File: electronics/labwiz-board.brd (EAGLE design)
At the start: 98.8 x 51 mm, 92 parts, among them J1 SD_MICRO_SDIO_1BIT, J2 CORTEX_DEBUGSMD, J3 DNP, U1 STM32F10XRXT6, U2 MCP73831, U4 MIC5219-3.3V, X2 M12_BOTTOM_CONTACTS_FPC_1MM, Y3 32.768kHz

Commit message: Updated .gitignore. Comitting unknown schematic updates.
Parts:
- removed J4: (no value), SparkFun-Connectors:1X03
- added TP10, TP8, TP9: DNP, PaxInstruments-Connectors:PAD_1MM
- moved BAT1 84.3 mm to (89.5, 16.7), turned to 90 degrees
- moved R19 19.9 mm to (37.0, 3.81), turned to 180 degrees
- moved U$6 18.6 mm to (48.6, 20.4)
- moved C3 14.6 mm to (91.1, 35.2), turned to 270 degrees
- moved TP3 13.0 mm to (83.9, 9.98)
- moved C31 7.63 mm to (8.08, 33.1)
- moved R15 7.63 mm to (8.08, 31.9)
- moved C30 4.57 mm to (8.08, 30.6)
- moved R16 4.57 mm to (8.08, 29.4)
- moved C35 4.28 mm to (37.0, 14.2), turned to 180 degrees
- moved R20 2.93 mm to (87.5, 35.2), turned to 90 degrees
- moved C36 2.89 mm to (37.0, 13.0), turned to 0 degrees
- moved C28 2.66 mm to (90.4, 18.3)
- moved R24 2.51 mm to (90.4, 17.1)
- moved C10 2.46 mm to (37.0, 11.7), turned to 0 degrees
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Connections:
- net GND: now also TP10.P$1; no longer J4.3
- net USART1_RX: now also TP9.P$1; no longer J4.2
- net USART1_TX: now also TP8.P$1; no longer J4.1
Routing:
- net LCD_BL: track 41.9 -> 18.0 mm
- net RTC_BAT: track 51.8 -> 70.1 mm, vias 1 -> 3
- net N$4: track 11.8 -> 25.7 mm
- net SWDIO: track 104.9 -> 117.3 mm
- net SWCLK: track 103.5 -> 115.2 mm
- net USART1_RX: track 107.5 -> 116.3 mm
- net I2C1_SCL: track 101.5 -> 109.4 mm
- net I2C1_SDA: track 101.5 -> 109.3 mm
- net USART2_TX: track 63.7 -> 71.5 mm, vias 5 -> 3
- net USART2_RX: track 57.2 -> 63.8 mm, vias 2 -> 4
- net SW_E_BOOT0: track 56.6 -> 50.2 mm
- net SW_A: track 113.3 -> 119.6 mm, vias 3 -> 5
- net N$38: track 4.33 -> 10.5 mm
- net N$37: track 4.76 -> 9.06 mm
- net NRST: track 125.7 -> 129.7 mm, vias 6 -> 5
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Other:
- outline, holes or cut-outs redrawn

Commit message: Updated MCP73831/2 name.
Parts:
- U2: value MCP73831 -> MCP73831/2
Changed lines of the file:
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@@
 <layer number="106" name="bPlate" color="7" fill="1" visible="yes" active="yes"/>
 <layer number="107" name="Crop" color="7" fill="1" visible="yes" active="yes"/>
+<layer number="108" name="tplace-old" color="7" fill="1" visible="yes" active="yes"/>
+<layer number="109" name="ref-old" color="7" fill="1" visible="yes" active="yes"/>
+<layer number="110" name="fp0" color="7" fill="1" visible="yes" active="yes"/>
+<layer number="111" name="LPC17xx" color="7" fill="1" visible="yes" active="yes"/>
+<layer number="112" name="tSilk" color="7" fill="1" visible="yes" active="yes"/>
+<layer number="113" name="ReferenceLS" color="7" fill="1" visible="yes" active="yes"/>
+<layer number="114" name="FRNTMAAT1" color="7" fill="1" visible="no" active="no"/>
+<layer number="115" name="FRNTMAAT2" color="7" fill="1" visible="no" active="no"/>
+<layer number="116" name="Patch_BOT" color="7" fill="1" visible="yes" active="yes"/>
 <layer number="117" name="BACKMAAT1" color="7" fill="1" visible="no" active="no"/>
+<layer number="118" name="Rect_Pads" color="7" fill="1" visible="yes" active="yes"/>
 <layer number="119" name="KAP_TEKEN" color="7" fill="1" visible="no" active="no"/>
 <layer number="120" name="KAP_MAAT1" color="7" fill="1" visible="no" active="no"/>
+<layer number="121" name="_tsilk" color="7" fill="1" visible="yes" active="yes"/>
+<layer number="122" name="_bsilk" color="7" fill="1" visible="yes" active="yes"/>
+<layer number="123" name="tTestmark" color="7" fill="1" visible="yes" active="yes"/>
+<layer number="124" name="bTestmark" color="7" fill="1" visible="yes" active="yes"/>
+<layer number="125" name="_tNames" color="7" fill="1" visible="yes" active="yes"/>
+<layer number="126" name="_bNames" color="7" fill="1" visible="yes" active="yes"/>
+<layer number="127" name="_tValues" color="7" fill="1" visible="yes" active="yes"/>
+<layer number="128" name="_bValues" color="7" fill="1" visible="yes" active="yes"/>
+<layer number="129" name="Mask" color="7" fill="1" visible="yes" active="yes"/>
 <layer number="130" name="SMDSTROOK" color="7" fill="1" visible="no" active="no"/>
+<layer number="131" name="tAdjust" color="7" fill="1" visible="yes" active="yes"/>
+<layer number="132" name="bAdjust" color="7" fill="1" visible="yes" active="yes"/>
 <layer number="133" name="bottom_silk" color="7" fill="1" visible="no" active="no"/>
+<layer number="144" name="Drill_legend" color="7" fill="1" visible="yes" active="yes"/>
+<layer number="150" name="Notes" color="7" fill="1" visible="yes" active="yes"/>
+<layer number="151" name="HeatSink" color="7" fill="1" visible="yes" active="yes"/>
+<layer number="152" name="_bDocu" color="7" fill="1" visible="yes" active="yes"/>
+<layer number="153" name="FabDoc1" color="7" fill="1" visible="yes" active="yes"/>
+<layer number="154" name="FabDoc2" color="7" fill="1" visible="yes" active="yes"/>
+<layer number="155" name="FabDoc3" color="7" fill="1" visible="yes" active="yes"/>
+<layer number="199" name="Contour" color="7" fill="1" visible="yes" active="yes"/>
+<layer number="200" name="200bmp" color="7" fill="1" visible="yes" active="yes"/>
+<layer number="201" name="201bmp" color="7" fill="1" visible="yes" active="yes"/>
+<layer number="202" name="202bmp" color="7" fill="1" visible="yes" active="yes"/>
+<layer number="203" name="203bmp" color="7" fill="1" visible="yes" active="yes"/>
+<layer number="204" name="204bmp" color="7" fill="1" visible="yes" active="yes"/>
+<layer number="205" name="205bmp" color="7" fill="1" visible="yes" active="yes"/>
+<layer number="206" name="206bmp" color="7" fill="1" visible="yes" active="yes"/>
+<layer number="207" name="207bmp" color="7" fill="1" visible="yes" active="yes"/>
+<layer number="208" name="208bmp" color="7" fill="1" visible="yes" active="yes"/>
+<layer number="209" name="209bmp" color="7" fill="1" visible="yes" active="yes"/>
+<layer number="210" name="210bmp" color="7" fill="1" visible="yes" active="yes"/>
+<layer number="211" name="211bmp" color="7" fill="1" visible="yes" active="yes"/>
+<layer number="212" name="212bmp" color="7" fill="1" visible="yes" active="yes"/>
+<layer number="213" name="213bmp" color="7" fill="1" visible="yes" active="yes"/>
+<layer number="214" name="214bmp" color="7" fill="1" visible="yes" active="yes"/>
+<layer number="215" name="215bmp" color="7" fill="1" visible="yes" active="yes"/>
+<layer number="216" name="216bmp" color="7" fill="1" visible="yes" active="yes"/>
 <layer number="217" name="217bmp" color="18" fill="1" visible="no" active="no"/>
 <layer number="218" name="218bmp" color="19" fill="1" visible="no" active="no"/>
@@
 <layer number="223" name="223bmp" color="24" fill="1" visible="no" active="no"/>
 <layer number="224" name="224bmp" color="25" fill="1" visible="no" active="no"/>
+<layer number="225" name="225bmp" color="7" fill="1" visible="yes" active="yes"/>
+<layer number="226" name="226bmp" color="7" fill="1" visible="yes" active="yes"/>
+<layer number="227" name="227bmp" color="7" fill="1" visible="yes" active="yes"/>
+<layer number="228" name="228bmp" color="7" fill="1" visible="yes" active="yes"/>
+<layer number="229" name="229bmp" color="7" fill="1" visible="yes" active="yes"/>
+<layer number="230" name="230bmp" color="7" fill="1" visible="yes" active="yes"/>
+<layer number="231" name="Eagle3D_PG1" color="7" fill="1" visible="yes" active="yes"/>
+<layer number="232" name="Eagle3D_PG2" color="7" fill="1" visible="yes" active="yes"/>
+<layer number="233" name="Eagle3D_PG3" color="7" fill="1" visible="yes" active="yes"/>
+<layer number="248" name="Housing" color="7" fill="1" visible="yes" active="yes"/>
+<layer number="249" name="Edge" color="7" fill="1" visible="yes" active="yes"/>
 <layer number="250" name="Descript" color="3" fill="1" visible="no" active="no"/>
 <layer number="251" name="SMDround" color="12" fill="11" visible="no" active="no"/>
+<layer number="254" name="cooling" color="7" fill="1" visible="yes" active="yes"/>
+<layer number="255" name="routoute" color="7" fill="1" visible="yes" active="yes"/>
 </layers>
 <board>
@@
 </element>
 <element name="U$9" library="PaxInstruments-FreqCtrl" package="NX3225GD" value="8MHz" x="33.8328" y="10.0584" smashed="yes" rot="R90"/>
-<element name="U2" library="PaxInstruments-PowerIC" package="SOT23-5" value="MCP73831" x="10.2108" y="2.286" smashed="yes" rot="R90">
+<element name="U2" library="PaxInstruments-PowerIC" package="SOT23-5" value="MCP73831/2" x="10.2108" y="2.286" smashed="yes" rot="R90">
 <attribute name="MPN" value="MCP73832T-2DCI/OT" x="10.2108" y="2.286" size="1.778" layer="27" rot="R90" display="off"/>
 <attribute name="MF" value="Microchip Technology" x="10.2108" y="2.286" size="1.778" layer="27" rot="R90" display="off"/>

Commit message: Swapped the net names for SW_D and SW_E. The physical locations were swapped on the v0.3 board.
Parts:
- R21: value 10K -> 2.32K (1%)
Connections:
- net SW_D_BOOT1 renamed SW_E_BOOT1
- net SW_E_BOOT0 renamed SW_D_BOOT0
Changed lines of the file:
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@@
 <attribute name="NAME" x="8.2296" y="2.286" size="0.5" layer="25" font="vector" align="center-left"/>
 </element>
-<element name="R21" library="PaxInstruments-RCL" package="0402" value="10K" x="14.3256" y="0.762" smashed="yes">
+<element name="R21" library="PaxInstruments-RCL" package="0402" value="2.32K (1%)" x="14.3256" y="0.762" smashed="yes">
 <attribute name="MPN" value="" x="14.3256" y="0.762" size="1.778" layer="27" display="off"/>
 <attribute name="POPULATE" value="" x="14.3256" y="0.762" size="1.778" layer="27" display="off"/>
@@
 <signal name="N$32">
 </signal>
-<signal name="SW_E_BOOT0">
+<signal name="SW_D_BOOT0">
 <contactref element="JP1" pad="1"/>
 <contactref element="U1" pad="29"/>
@@
 <wire x1="27.8892" y1="2.286" x2="51.5112" y2="2.286" width="0.1524" layer="16"/>
 </signal>
-<signal name="SW_D_BOOT1">
+<signal name="SW_E_BOOT1">
 <contactref element="U1" pad="28"/>
 <contactref element="R16" pad="2"/>

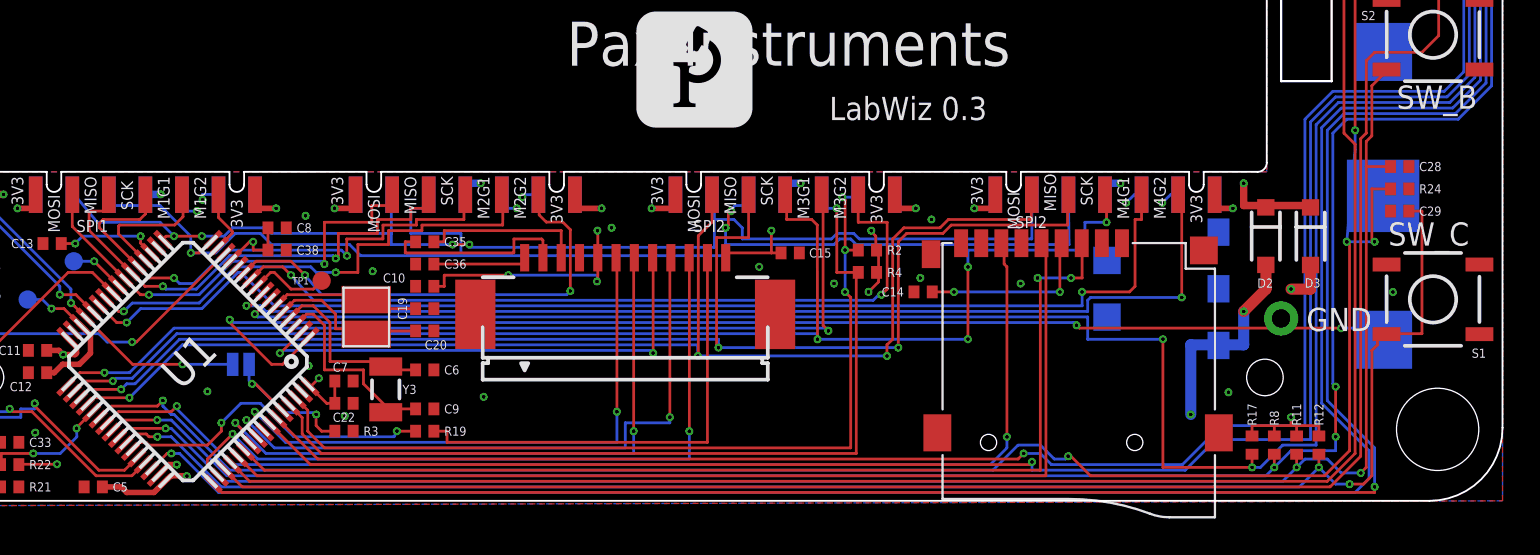
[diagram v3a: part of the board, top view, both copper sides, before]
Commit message: Swapped WIFI_EN with SW_A to avoid interrupt sharing.
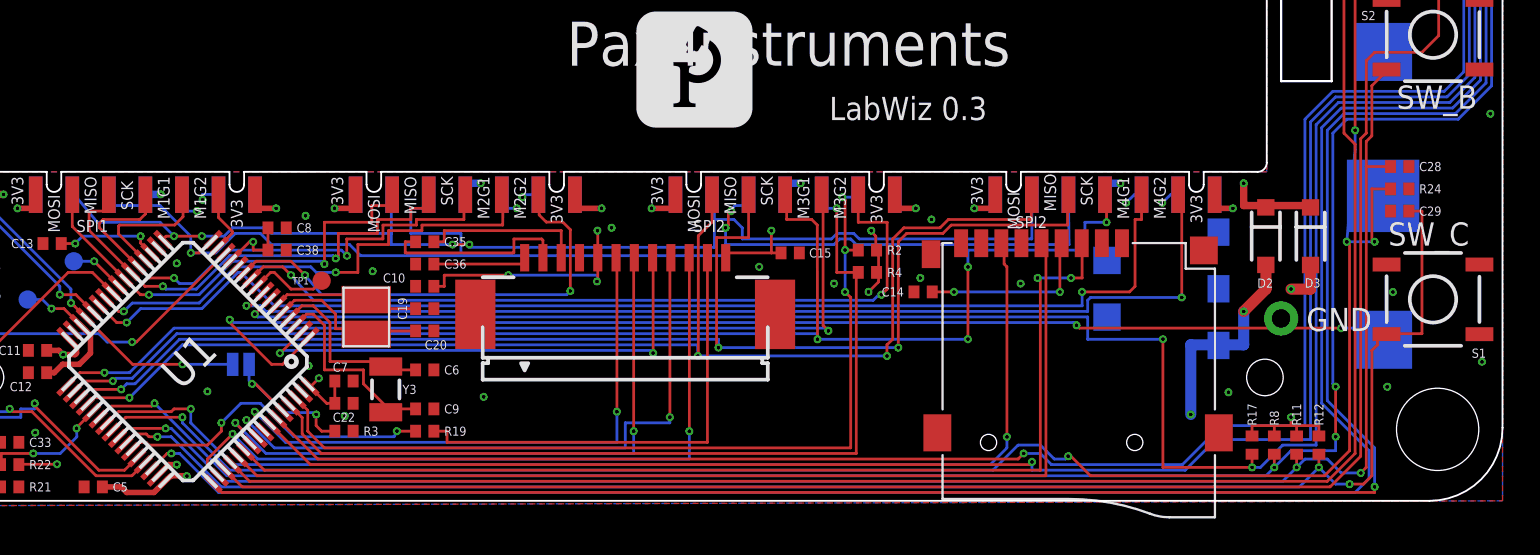
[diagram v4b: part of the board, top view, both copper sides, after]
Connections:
- net SW_A: now also U1.38; no longer U1.40
- net WIFI_EN: now also U1.40; no longer U1.38
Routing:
- net SW_A: track 119.6 -> 120.8 mm
- net WIFI_EN: track 108.7 -> 107.5 mm
- net GND: vias 23 -> 27

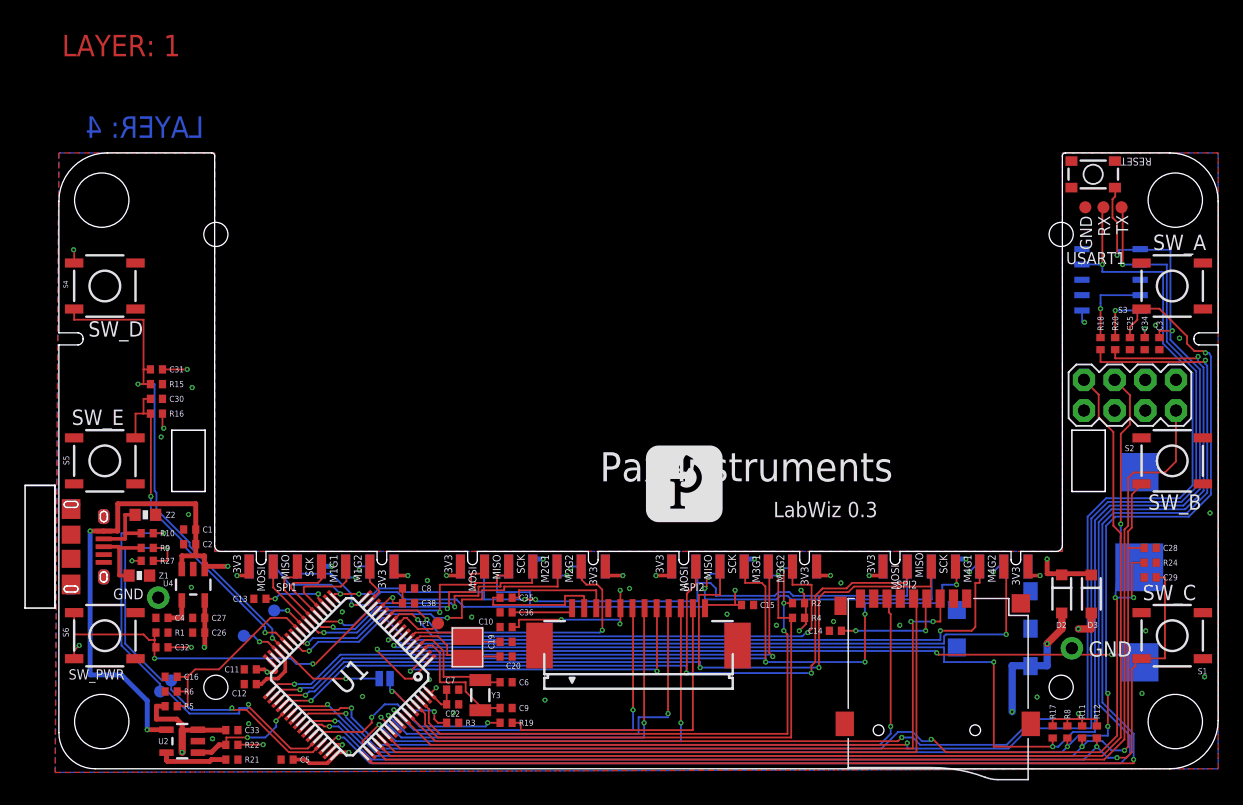
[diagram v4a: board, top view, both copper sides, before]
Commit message: Added a PTC fuse. #59.
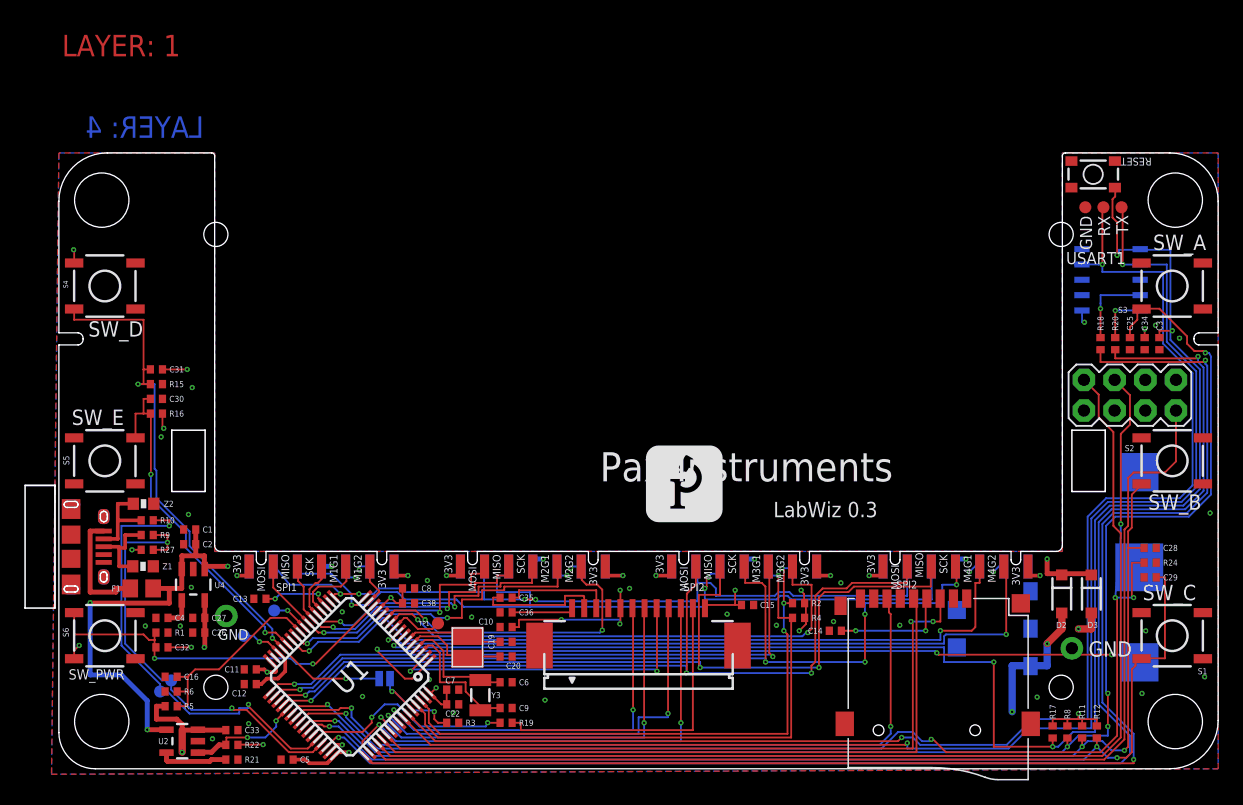
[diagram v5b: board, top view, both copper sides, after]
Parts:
- added F1: 1000mA, PaxInstruments-RCL:0805
- moved TP4 5.84 mm to (13.9, 12.6)
- moved R10 1.07 mm to (7.32, 20.6)
- moved R9 1.07 mm to (7.32, 19.4)
- moved Z2 0.93 mm to (7.01, 21.9)
- moved R27 0.91 mm to (7.32, 18.1)
- moved Z1 0.82 mm to (6.97, 16.8)
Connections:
- new net USB_VCC: F1.1, U$1.PIN$1
- net VBUS: now also F1.2; no longer U$1.PIN$1
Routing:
- net USB_VCC: track 0.00 -> 9.80 mm
- net VBUS: track 130.6 -> 123.3 mm
- net SPI1_SCK: track 29.5 -> 27.2 mm
- net USB_DM: track 35.1 -> 37.1 mm
- net D-: track 5.92 -> 7.30 mm
- net SPI1_MISO: track 27.0 -> 25.7 mm
- net MOD1_GPIO1: track 7.33 -> 6.02 mm
- net USB_DP: track 35.6 -> 36.2 mm
- net D+: track 6.32 -> 6.93 mm
- net GND: vias 27 -> 29

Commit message: Added transient voltage suppressor to USB_VCC. Closes #59.
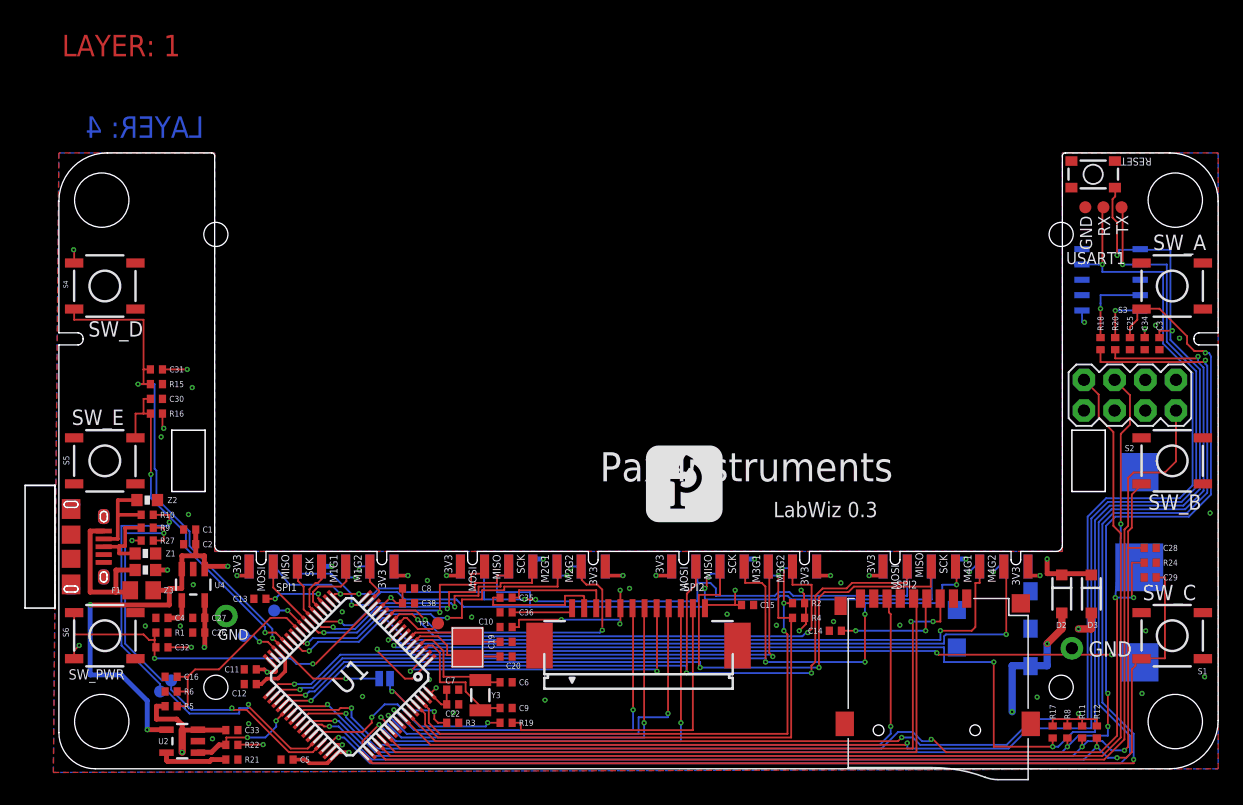
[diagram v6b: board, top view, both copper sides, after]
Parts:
- added Z3: PGB1010603, PaxInstrument-T400:SPARKFUN-RESISTORS_0603-RES
- moved Z1 1.08 mm to (7.16, 17.8)
- moved R27 0.76 mm to (7.32, 18.9)
- moved R9 0.61 mm to (7.32, 20.0)
- moved R10 0.46 mm to (7.32, 21.0)
- moved Z2 0.43 mm to (7.32, 22.3)
- moved F1 0.15 mm to (6.86, 14.8)
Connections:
- net GND: now also Z3.1
- net USB_VCC: now also Z3.2
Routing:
- net USB_VCC: track 9.80 -> 13.1 mm
- net GND: track 1.42 -> 2.40 mm, vias 29 -> 30
- net D-: track 7.30 -> 7.91 mm
